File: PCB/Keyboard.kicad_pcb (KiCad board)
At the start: 2 copper layers, 28 x 18 mm, 25 parts, among them P1 USB_OTG, SW1 RST, U1 ATMEGA32U4-QFN44, X1 ABM10-16.000MHZ-D30-T3

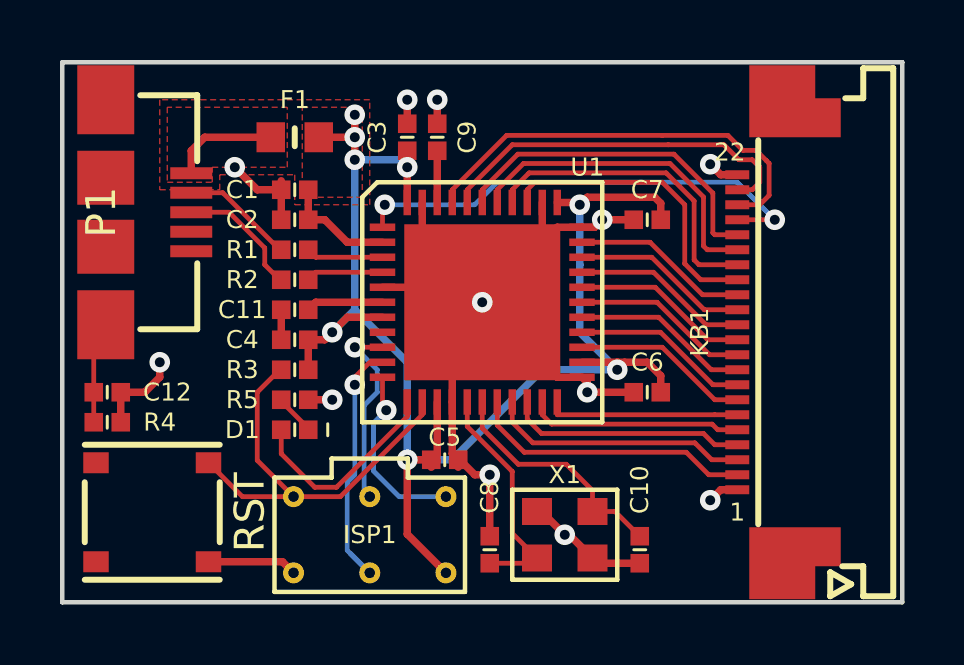
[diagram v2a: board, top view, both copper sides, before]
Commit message: Switched to new library names
At least for the PCB
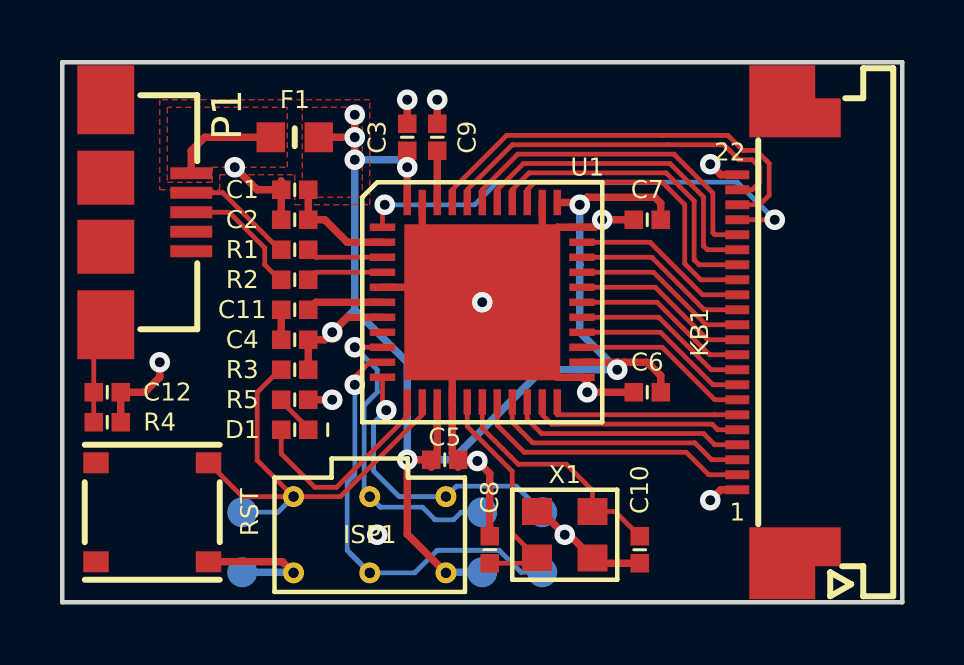
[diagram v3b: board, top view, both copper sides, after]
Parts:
- added J1: RESET, RB-SMD-Connectors:TESTPOINT-1mm-NO_TEXT, B.Cu at (155.0, 113.0)
- added J2: SCK, RB-SMD-Connectors:TESTPOINT-1mm-NO_TEXT, B.Cu at (163.0, 113.0)
- added J23: 5V, RB-SMD-Connectors:TESTPOINT-1mm-NO_TEXT, B.Cu at (163.0, 115.0)
- added J26: GND, RB-SMD-Connectors:TESTPOINT-1mm-NO_TEXT, B.Cu at (155.0, 115.0)
- added J3: MISO, RB-SMD-Connectors:TESTPOINT-1mm-NO_TEXT, B.Cu at (165.0, 113.0)
- added J4: MOSI, RB-SMD-Connectors:TESTPOINT-1mm-NO_TEXT, B.Cu at (165.0, 115.0)
- C1, C10, C11, C12, C2, C3, C4, C5, C6, C7, C8, C9: footprint SMD-DiscreteB:C-0402-1005 -> RB-SMD-DiscreteB:C-0402-1005
- D1: footprint SMD-DiscreteB:LED-0402-1005 -> RB-SMD-DiscreteB:LED-0402-1005
- F1: footprint SMD-DiscreteB:F-0603-1608 -> RB-SMD-DiscreteB:F-0603-1608
- KB1: footprint SMD-Connectors:FPC_0.5mm_22p-MOLEX_52437 -> RB-SMD-Connectors:FPC_0.5mm_22p-MOLEX_52437
- P1: footprint SMD-Connectors:USB-MICRO-10104110-0001LF -> RB-SMD-Connectors:USB-MICRO-10104110-0001LF
- R1, R2, R3, R4, R5: footprint SMD-DiscreteB:R-0402-1005 -> RB-SMD-DiscreteB:R-0402-1005
- SW1: footprint SMD-Switches:ALPS-SKRMAAE010 -> RB-SMD-Switches:ALPS-SKRMAAE010
- U1: footprint SMD-QFN:VQFN-44_ATMEL -> RB-SMD-QFN:VQFN-44_ATMEL
- X1: footprint SMD-XTAL:2.5x2mm -> RB-SMD-XTAL:2.5x2mm
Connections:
- P1 pad 4: (no net) -> Net-(P1-Pad4)
- U1 pad 8: (no net) -> /TMP
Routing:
- net /MOSI: track 10.4 -> 16.8 mm
- net /SCK: track 6.79 -> 11.0 mm
- net /MISO: track 6.12 -> 9.84 mm
- net /RESET: track 14.2 -> 16.2 mm
- net GND: track 53.1 -> 54.9 mm, vias 12 -> 13
- net +5V: track 55.2 -> 56.4 mm
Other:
- board text added: "USB Keyboard v1.22 RasmusB 2018 Psion Series 5/5mx"
- board text removed: "USB Keyboard v1.1 RasmusB 2017 Psion Series 5/5mx"

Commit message: Added test points
For ICSP and USB. Keyboard connections are tested through a flex cable. LEDs are tested visually.
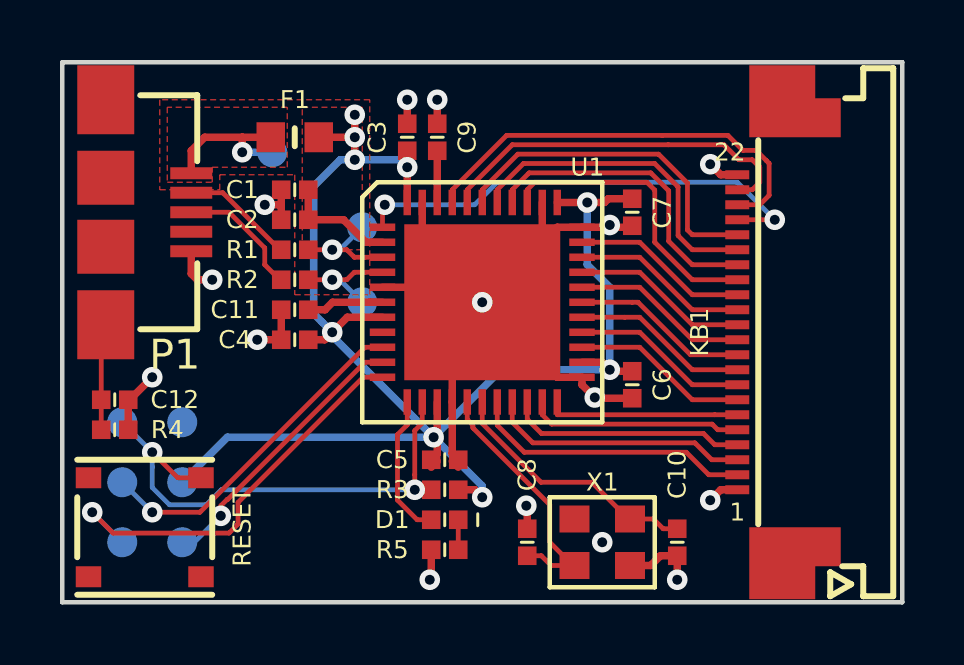
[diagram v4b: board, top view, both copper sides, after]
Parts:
- removed ISP1: ATMEL_ISP-6P, SMD-Connectors:ISP-PADS_2mm54
- added J5: D-, RB-SMD-Connectors:TESTPOINT-1mm-NO_TEXT, B.Cu at (159.0, 103.5)
- added J6: D+, RB-SMD-Connectors:TESTPOINT-1mm-NO_TEXT, B.Cu at (159.0, 106.0)
- added J7: VBUS, RB-SMD-Connectors:TESTPOINT-1mm-NO_TEXT, B.Cu at (156.0, 101.0)
- SW1: value RST -> RESET
- moved J3 14.0 mm to (151.0, 114.0), turned to 180 degrees
- moved J2 12.0 mm to (151.0, 112.0), turned to 180 degrees
- moved J4 12.0 mm to (153.0, 114.0), turned to 180 degrees
- moved J23 10.4 mm to (153.0, 112.0), turned to 180 degrees
- moved R5 7.07 mm to (161.8, 114.2), turned to 0 degrees
- moved R3 6.40 mm to (161.8, 112.2)
- moved D1 5.83 mm to (161.8, 113.2)
- moved J26 5.39 mm to (153.0, 110.0), turned to 180 degrees
- moved J1 5.00 mm to (151.0, 110.0), turned to 180 degrees
- moved C10 1.27 mm to (169.5, 114.0)
- moved C8 1.27 mm to (164.5, 114.0)
- moved X1 1.27 mm to (167.0, 114.0)
- moved C6 0.56 mm to (168.0, 108.8), turned to 270 degrees
- moved C7 0.56 mm to (168.0, 103.0), turned to 270 degrees
- moved SW1 0.56 mm to (151.8, 113.5)
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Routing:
- net GND: track 54.9 -> 45.5 mm, vias 13 -> 15
- net /MOSI: track 16.8 -> 9.36 mm
- net /MISO: track 9.84 -> 14.0 mm
- net /LED: track 7.35 -> 5.23 mm
- net VBUS: track 3.59 -> 5.09 mm, vias 0 -> 1
- net /D-: track 2.58 -> 3.89 mm, vias 0 -> 1
- net /D+: track 2.58 -> 3.89 mm, vias 0 -> 1
- net /RESET: track 16.2 -> 17.3 mm, vias 0 -> 2
- net Net-(C8-Pad1): track 7.81 -> 8.67 mm
- net Net-(C10-Pad1): track 8.03 -> 8.67 mm
- net +5V: track 56.4 -> 56.7 mm, vias 8 -> 9

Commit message: Final fixes
Re-annotation, version numbering of schematic
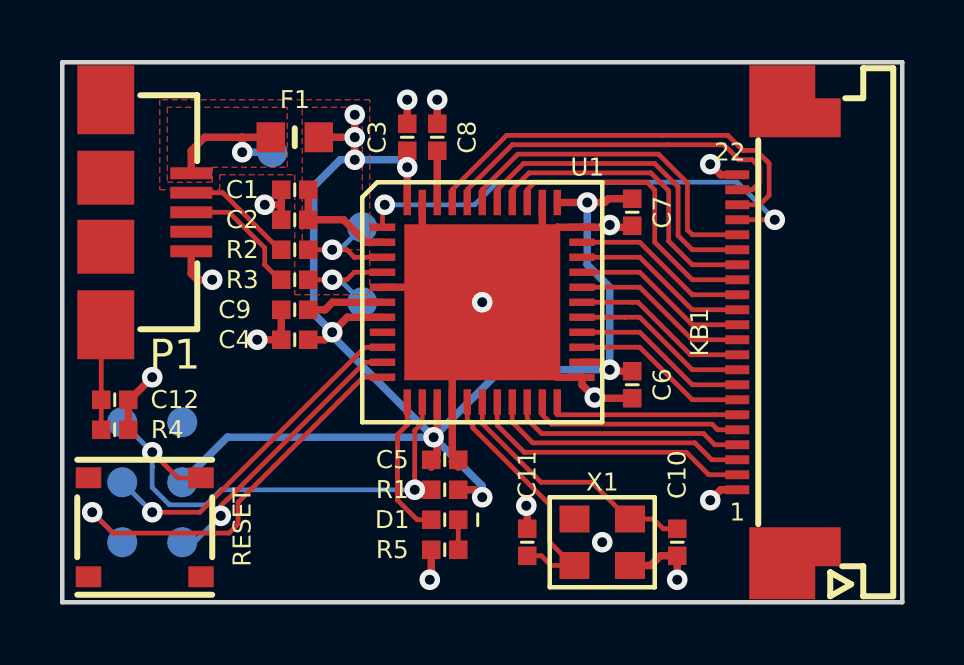
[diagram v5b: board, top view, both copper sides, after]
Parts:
- renumbered C8 to C11, C9 to C8, C11 to C9, J7 to J5, J23 to J6, J5 to J7, J6 to J8, J26 to J9, R3 to R1, R1 to R2, R2 to R3

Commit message: Adjustments to PCB
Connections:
- KB1 pad 4: /COL_10 -> /COL_11
- KB1 pad 5: /COL_11 -> /COL_10
- U1 pad 20: /COL_10 -> /COL_11
- U1 pad 21: /COL_11 -> /COL_10
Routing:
- net /COL_11: track 7.13 -> 7.93 mm
- net /COL_10: track 7.93 -> 7.13 mm
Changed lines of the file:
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@@
   (module RB-SMD-Connectors:FPC_0.5mm_22p-MOLEX_52437 (layer F.Cu)
     (at 171.5 107 90)
+    (attr smd)
     (fp_text reference KB1 (at 0 -1.25 270) (layer F.SilkS)
       (effects (font (size 0.6 0.6) (thickness 0.1)))
@@
       (net 2 /COL_8))
     (pad 5 smd rect (at -3.25 0 90) (size 0.3 0.8) (layers F.Cu F.Paste F.Mask)
+      (net 28 /COL_10))
+    (pad 4 smd rect (at -3.75 0 90) (size 0.3 0.8) (layers F.Cu F.Paste F.Mask)
       (net 29 /COL_11))
-    (pad 4 smd rect (at -3.75 0 90) (size 0.3 0.8) (layers F.Cu F.Paste F.Mask)
-      (net 28 /COL_10))
     (pad 3 smd rect (at -4.25 0 90) (size 0.3 0.8) (layers F.Cu F.Paste F.Mask)
       (net 27 /COL_12))
@@
       (net 2 /COL_8) (solder_mask_margin 0.05) (solder_paste_margin -0.015))
     (pad 21 smd rect (at 3.325 -2) (size 0.25 0.85) (layers F.Cu F.Paste F.Mask)
+      (net 28 /COL_10) (solder_mask_margin 0.05) (solder_paste_margin -0.015))
+    (pad 20 smd rect (at 3.325 -1.5) (size 0.25 0.85) (layers F.Cu F.Paste F.Mask)
       (net 29 /COL_11) (solder_mask_margin 0.05) (solder_paste_margin -0.015))
-    (pad 20 smd rect (at 3.325 -1.5) (size 0.25 0.85) (layers F.Cu F.Paste F.Mask)
-      (net 28 /COL_10) (solder_mask_margin 0.05) (solder_paste_margin -0.015))
     (pad 19 smd rect (at 3.325 -1) (size 0.25 0.85) (layers F.Cu F.Paste F.Mask)
       (net 27 /COL_12) (solder_mask_margin 0.05) (solder_paste_margin -0.015))
@@
   (module RB-SMD-Switches:ALPS-SKRMAAE010 (layer F.Cu)
     (at 151.75 113.5 90)
+    (attr smd)
     (fp_text reference SW1 (at 0.5 0 90) (layer F.SilkS) hide
       (effects (font (size 1 1) (thickness 0.15)))
     )
-    (fp_text value RESET (at 0 3.25 90) (layer F.SilkS)
+    (fp_text value RESET (at 0 3.25 90) (layer F.Fab)
       (effects (font (size 0.6 0.6) (thickness 0.1)))
     )
@@
   (module RB-SMD-Connectors:USB-MICRO-10104110-0001LF (layer F.Cu)
     (at 149 103 270)
+    (attr smd)
     (fp_text reference P1 (at 4.75 -3.75 180) (layer F.SilkS)
       (effects (font (size 1 1) (thickness 0.15)))
@@
   (segment (start 164.687206 110.687206) (end 170.087206 110.687206) (width 0.16) (layer F.Cu) (net 27))
   (segment (start 164 110) (end 164.687206 110.687206) (width 0.16) (layer F.Cu) (net 27))
-  (segment (start 164.5 109.325) (end 164.5 109.9) (width 0.16) (layer F.Cu) (net 28))
-  (segment (start 170.75 110.75) (end 171.5 110.75) (width 0.16) (layer F.Cu) (net 28))
-  (segment (start 170.374804 110.374804) (end 170.75 110.75) (width 0.16) (layer F.Cu) (net 28))
-  (segment (start 164.974804 110.374804) (end 170.374804 110.374804) (width 0.16) (layer F.Cu) (net 28))
-  (segment (start 164.5 109.9) (end 164.974804 110.374804) (width 0.16) (layer F.Cu) (net 28))
-  (segment (start 165 109.325) (end 165 109.75) (width 0.16) (layer F.Cu) (net 29))
-  (segment (start 165 109.75) (end 165.312402 110.062402) (width 0.16) (layer F.Cu) (net 29))
-  (segment (start 165.312402 110.062402) (end 170.662402 110.062402) (width 0.16) (layer F.Cu) (net 29))
-  (segment (start 170.662402 110.062402) (end 170.85 110.25) (width 0.16) (layer F.Cu) (net 29))
-  (segment (start 170.85 110.25) (end 171.5 110.25) (width 0.16) (layer F.Cu) (net 29))
+  (segment (start 165 109.325) (end 165 109.75) (width 0.16) (layer F.Cu) (net 28))
+  (segment (start 165 109.75) (end 165.312402 110.062402) (width 0.16) (layer F.Cu) (net 28))
+  (segment (start 165.312402 110.062402) (end 170.662402 110.062402) (width 0.16) (layer F.Cu) (net 28))
+  (segment (start 170.662402 110.062402) (end 170.85 110.25) (width 0.16) (layer F.Cu) (net 28))
+  (segment (start 170.85 110.25) (end 171.5 110.25) (width 0.16) (layer F.Cu) (net 28))
+  (segment (start 164.5 109.325) (end 164.5 109.9) (width 0.16) (layer F.Cu) (net 29))
+  (segment (start 170.75 110.75) (end 171.5 110.75) (width 0.16) (layer F.Cu) (net 29))
+  (segment (start 170.374804 110.374804) (end 170.75 110.75) (width 0.16) (layer F.Cu) (net 29))
+  (segment (start 164.974804 110.374804) (end 170.374804 110.374804) (width 0.16) (layer F.Cu) (net 29))
+  (segment (start 164.5 109.9) (end 164.974804 110.374804) (width 0.16) (layer F.Cu) (net 29))
   (segment (start 150.45 106.75) (end 150.45 106.95) (width 0.16) (layer F.Cu) (net 30))
   (segment (start 150.3 106.9) (end 150.45 106.75) (width 0.16) (layer F.Cu) (net 30))

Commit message: Version 1.3 produced
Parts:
- removed X1: ABM10-16.000MHZ-D30-T3, RB-SMD-XTAL:2.5x2mm
- added Y1: 16MHz, Crystal:Crystal_SMD_Abracon_ABM10-4Pin_2.5x2.0mm, F.Cu at (166.8, 113.8)
- C1, C9: value 1µ -> 1uF; footprint RB-SMD-DiscreteB:C-0402-1005 -> Capacitor_SMD:C_0402_1005Metric
- C10, C11: value 15p -> 6.2pF; footprint RB-SMD-DiscreteB:C-0402-1005 -> Capacitor_SMD:C_0402_1005Metric
- C12: value 4n7 -> 4.7nF; footprint RB-SMD-DiscreteB:C-0402-1005 -> Capacitor_SMD:C_0402_1005Metric
- C2, C3, C4, C5, C6, C7, C8: value 100n -> 100nF; footprint RB-SMD-DiscreteB:C-0402-1005 -> Capacitor_SMD:C_0402_1005Metric
- D1: footprint RB-SMD-DiscreteB:LED-0402-1005 -> LED_SMD:LED_0402_1005Metric
- F1: footprint RB-SMD-DiscreteB:F-0603-1608 -> Fuse:Fuse_0603_1608Metric
- KB1: footprint RB-SMD-Connectors:FPC_0.5mm_22p-MOLEX_52437 -> USB-Keyboard-Adapter-LIBRARY:FPC_22p-JUSHUO_AFC01-S22FCC-00
- P1: footprint RB-SMD-Connectors:USB-MICRO-10104110-0001LF -> Connector_USB:USB_Micro-B_Amphenol_10118194_Horizontal
- R1, R2, R3, R4, R5: footprint RB-SMD-DiscreteB:R-0402-1005 -> Resistor_SMD:R_0402_1005Metric
- U1: footprint RB-SMD-QFN:VQFN-44_ATMEL -> Package_DFN_QFN:QFN-44-1EP_7x7mm_P0.5mm_EP5.2x5.2mm
- moved P1 2.78 mm to (151.8, 103.0)
- moved SW1 1.06 mm to (152.5, 112.8)
- moved C12 0.79 mm to (151.0, 108.5)
- moved R4 0.79 mm to (151.0, 109.5)
- moved KB1 0.43 mm to (171.1, 107.0)
- moved C11 0.36 mm to (164.2, 114.2), turned to -90 degrees
- moved C10 0.25 mm to (169.2, 114.0)
- turned U1 to 0 degrees
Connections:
- P1 pad 4: Net-(P1-Pad4) -> unconnected-(P1-Pad4)
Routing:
- net GNDPWR: track 3.76 -> 16.2 mm
- net GND: track 45.5 -> 36.1 mm, vias 15 -> 16
- net +5V: track 56.7 -> 62.8 mm
- net /SCK: track 11.4 -> 13.4 mm
- net /MISO: track 14.0 -> 12.0 mm
- net /COL_8: track 6.60 -> 5.57 mm
- net /ROW_01: track 12.5 -> 13.3 mm
- net Net-(C11-Pad1): track 8.67 -> 7.98 mm
- net /ROW_08: track 14.4 -> 15.1 mm
- net /RESET: track 17.3 -> 17.9 mm
- net VBUS: track 5.09 -> 4.55 mm
- net /ROW_05: track 10.3 -> 9.81 mm
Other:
- net class Default removed
- net class Power removed
- rule pad_to_mask_clearance: 0.05 -> 0
- board text added: "USB Keyboard v1.3 RasmusB 2022 Psion Series 5/5mx"
- board text removed: "USB Keyboard v1.22 RasmusB 2018 Psion Series 5/5mx"
